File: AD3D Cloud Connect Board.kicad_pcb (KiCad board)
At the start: 2 copper layers, 65 x 31 mm, 19 parts, among them J1 Conn_02x20_Odd_Even, J2 502585-04771, J3 Conn_01x03, J4 502585-04771, J5 Conn_01x03, J6 Conn_01x03, P1 NPTC202KFMS-RC, SW1 Reprint, SW2 Next, SW3 Unload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

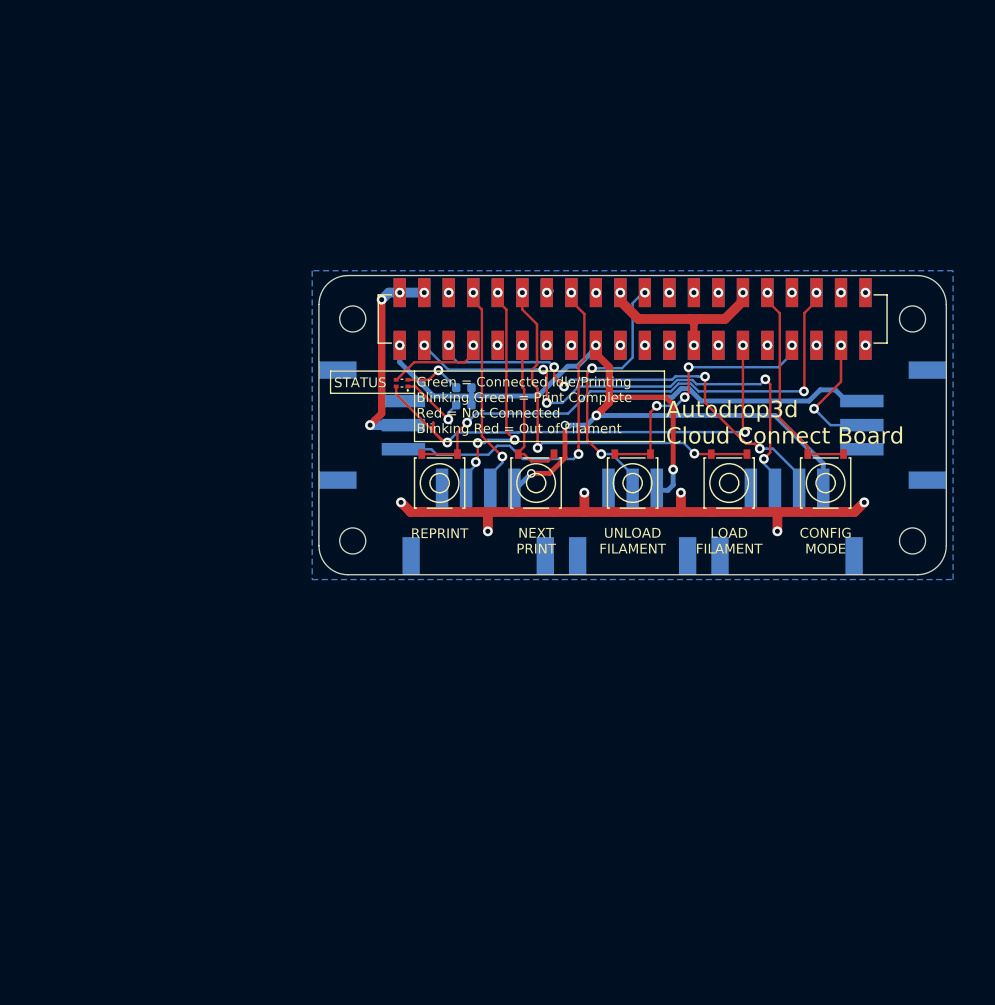
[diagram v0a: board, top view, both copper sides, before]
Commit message: Revision 1. Fixed button orientations split out LEDs Changed to standard 0.1" headers
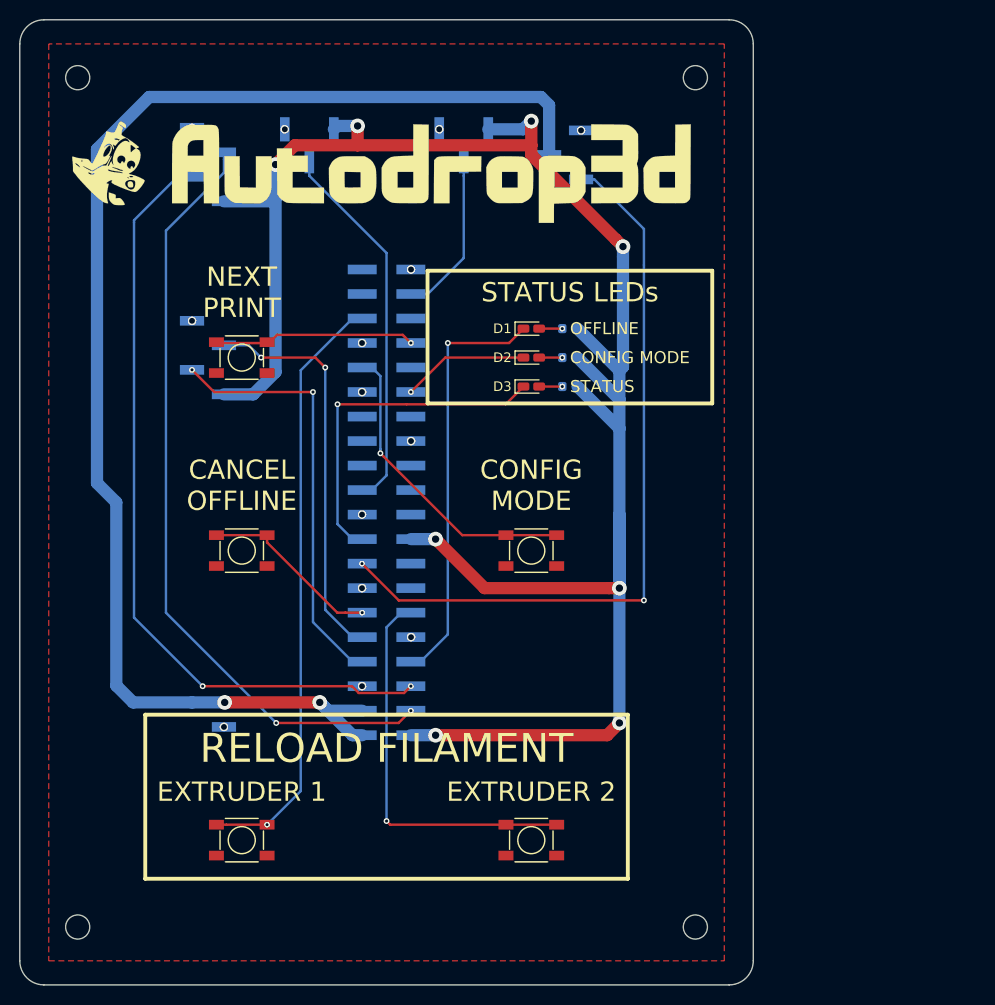
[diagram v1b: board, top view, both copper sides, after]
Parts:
- removed J1: Conn_02x20_Odd_Even, AD3D custom footprints:95157-440LF
- added D2: 150060VS75000, Diode_SMD:D_0603_1608Metric_Castellated, F.Cu at (222.0, 124.0)
- added D3: 150060RS75000, Diode_SMD:D_0603_1608Metric_Castellated, F.Cu at (222.0, 127.0)
- added G***: LOGO, AD3D custom footprints:AD3Dlogo, F.Cu at (206.4, 104.7)
- added J7: Conn_01x02, Connector_PinHeader_2.54mm:PinHeader_1x02_P2.54mm_Vertical_SMD_Pin1Right, B.Cu at (188.5, 161.0)
- added R1: 82 OHM 5%, Resistor_SMD:R_0603_1608Metric, B.Cu at (226.0, 127.0)
- D1: value APHB1608CGKSURKC -> 150060RS75000; footprint SamacSys_Parts:APHB1608CGKSURKC -> Diode_SMD:D_0603_1608Metric_Castellated
- J2, J4: value 502585-04771 -> Conn_01x04; footprint AD3D custom footprints:S4B-XH-SM4-TB -> Connector_PinHeader_2.54mm:PinHeader_1x04_P2.54mm_Vertical_SMD_Pin1Right
- J3, J5, J6: footprint AD3D custom footprints:S3B-XH-SM4-TB -> Connector_PinHeader_2.54mm:PinHeader_1x03_P2.54mm_Vertical_SMD_Pin1Right
- MK1, MK2, MK3, MK4: footprint MountingHole:MountingHole_2.7mm_M2.5 -> MountingHole:MountingHole_2.5mm
- P1: footprint AD3D custom footprints:NPTC202KFMS-RC -> Connector_PinSocket_2.54mm:PinSocket_2x20_P2.54mm_Vertical_SMD
- SW1: value Reprint -> Config; footprint AD3D custom footprints:PTS526-SK15-SMTR2-LFS -> AD3D custom footprints:SW_SPST_PTS647
- SW2: value Next -> Cancel/Offline; footprint AD3D custom footprints:PTS526-SK15-SMTR2-LFS -> AD3D custom footprints:SW_SPST_PTS647
- SW3: value Unload -> Next; footprint AD3D custom footprints:PTS526-SK15-SMTR2-LFS -> AD3D custom footprints:SW_SPST_PTS647
- SW4: value Load -> Flmnt 1; footprint AD3D custom footprints:PTS526-SK15-SMTR2-LFS -> AD3D custom footprints:SW_SPST_PTS647
- SW5: value Config -> Flmnt 2; footprint AD3D custom footprints:PTS526-SK15-SMTR2-LFS -> AD3D custom footprints:SW_SPST_PTS647
- moved J2 69.5 mm to (188.5, 104.0), turned to 0 degrees
- moved J5 52.3 mm to (215.0, 102.0), turned to 90 degrees
- moved SW4 51.0 mm to (192.0, 144.0), turned to 0 degrees
- moved J3 50.7 mm to (199.0, 102.0), turned to 90 degrees
- moved MK3 49.1 mm to (175.0, 183.0)
- moved MK4 45.9 mm to (239.0, 183.0)
- moved SW3 42.5 mm to (192.0, 124.0), turned to 0 degrees
- moved SW1 42.3 mm to (192.0, 174.0), turned to 0 degrees
- moved MK1 37.9 mm to (175.0, 95.0), turned to 0 degrees
- moved SW2 37.0 mm to (222.0, 174.0), turned to 0 degrees
- moved J6 33.8 mm to (225.5, 103.0), turned to 0 degrees
- moved MK2 33.6 mm to (239.0, 95.0), turned to 0 degrees
- moved P1 31.8 mm to (207.0, 139.0)
- moved J4 31.8 mm to (188.5, 124.0), turned to 0 degrees
- moved SW5 31.3 mm to (222.0, 144.0), turned to 0 degrees
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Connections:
- D1 pad 1: Net-(D1-Pad1) -> /GPIO4(GCLK)
- D1 pad 2: /GPIO5 -> Net-(D1-Pad2)
- R7 pad 1: Net-(D1-Pad3) -> Net-(D1-Pad2)
- R8 pad 2: Net-(D1-Pad1) -> Net-(D2-Pad2)
- SW1 pad 2: GND -> /GPIO16
- SW1 pad 3: /GPIO16 -> GND
- SW2 pad 2: GND -> /GPIO17(GEN0)
- SW2 pad 3: /GPIO17(GEN0) -> GND
- SW3 pad 2: GND -> /GPIO13(PWM1)
- SW3 pad 3: /GPIO13(PWM1) -> GND
- SW4 pad 2: GND -> /GPIO18(GEN1)(PWM0)
- SW4 pad 3: /GPIO18(GEN1)(PWM0) -> GND
- SW5 pad 2: GND -> /GPIO12(PWM0)
- SW5 pad 3: /GPIO12(PWM0) -> GND
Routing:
- net +5V: track 22.0 -> 143.4 mm, vias 4 -> 2
- net +3V3: track 129.2 -> 208.4 mm, vias 6 -> 8
- net GND: track 76.9 -> 0.00 mm
- net /GPIO23(GEN4): track 37.1 -> 77.9 mm
- net /GPIO5: track 50.7 -> 13.1 mm, vias 3 -> 1
- net /GPIO24(GEN5): track 0.03 -> 35.6 mm
- net /GPIO3(SCL1): track 47.0 -> 81.3 mm, vias 5 -> 2
- net /GPIO4(GCLK): track 9.98 -> 43.6 mm
- net /GPIO2(SDA1): track 53.4 -> 80.8 mm, vias 5 -> 2
- net /GPIO17(GEN0): track 16.0 -> 41.0 mm
- net /GPIO14(TXD0): track 22.2 -> 44.1 mm
- net /GPIO18(GEN1)(PWM0): track 39.5 -> 19.4 mm, vias 3 -> 1
- net /GPIO15(RXD0): track 25.3 -> 41.6 mm, vias 4 -> 2
- net /GPIO25(GEN6): track 27.5 -> 39.0 mm, vias 3 -> 0
- net /GPIO12(PWM0): track 22.2 -> 32.9 mm
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- added copper zone on F.Cu, net GND
- removed copper zone on B.Cu, net GND
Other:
- board size 65 x 31 mm -> 76 x 100 mm
- board text added: "3V3"
- board text added: "5V"
- board text added: "CANCEL OFFLINE"
- board text added: "D1 = GPIO4"
- board text added: "D2 = GPIO5"
- board text added: "D3 = GPIO24"
- board text added: "EXTRUDER 1"
- board text added: "EXTRUDER 2"
- board text added: "Filament 1"
- board text added: "Filament 2"
- board text added: "GND"
- board text added: "GPIO14"
- board text added: "GPIO15"
- board text added: "GPIO2"
- board text added: "GPIO23"
- board text added: "GPIO25"
- board text added: "GPIO26"
- board text added: "GPIO3"
- board text added: "I2C / GPIO"
- board text added: "Motor Ctrlr"
- board text added: "OFFLINE"
- board text added: "Power"
- board text added: "RELOAD FILAMENT"
- board text added: "STATUS LEDs"
- board text added: "Serial / GPIO"
- board text removed: "Autodrop3d Cloud Connect Board"
- board text removed: "Filament1"
- board text removed: "Filament2"
- board text removed: "Green = Connected Idle/Printing Blinking Green = Print Complete Red = Not Connected Blinking Red = Out of Filament"
- board text removed: "I2C"
- board text removed: "LOAD FILAMENT"
- board text removed: "Motor"
- board text removed: "RASPBERRY-PI 40-PIN ADDON BOARD VIEW FROM TOP NOTE: P1 SHOULD BE FITTED ON THE REVERSE OF THE BOARD"
- board text removed: "REPRINT"
- board text removed: "RXD"
- board text removed: "Rev: 0 P/N: AD-CCB-01"
- board text removed: "SCL"
- board text removed: "SDA"
- board text removed: "TXD"
- board text removed: "UART"
- board text removed: "UNLOAD FILAMENT"
